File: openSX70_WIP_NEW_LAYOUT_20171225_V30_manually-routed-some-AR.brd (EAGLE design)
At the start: 95.9 x 27.9 mm, 37 parts, among them Q1 5.8A/30V/35mΩ, Q2 5.8A/30V/35mΩ, U1 ATMEGA328P_TQFP, U3 BH1750FVI-TR, Y1 CSTCE16M0V53-R0

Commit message: Added some vias.
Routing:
- net GND: vias 14 -> 17
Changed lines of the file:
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@@
 <via x="24.638" y="21.971" extent="1-16" drill="0.35"/>
 <via x="20.193" y="22.606" extent="1-16" drill="0.35"/>
-<wire x1="67.095" y1="24.169" x2="61.302" y2="26.543" width="0" layer="19" extent="1-1"/>
+<via x="64.643" y="8.636" extent="1-16" drill="0.35"/>
+<via x="70.993" y="15.621" extent="1-16" drill="0.35"/>
+<via x="64.643" y="21.971" extent="1-16" drill="0.35"/>
+<wire x1="64.643" y1="21.971" x2="60.325" y2="23.495" width="0" layer="19" extent="1-1"/>
+<wire x1="67.095" y1="21.59" x2="64.643" y2="21.971" width="0" layer="19" extent="1-1"/>
 <wire x1="74.9935" y1="22.4155" x2="74.295" y2="26.035" width="0" layer="19" extent="1-1"/>
-<wire x1="82.423" y1="18.161" x2="76.47" y2="22.545" width="0" layer="19" extent="1-1"/>
-<wire x1="77.26914375" y1="13.5612" x2="78.400515625" y2="12.429828125" width="0" layer="19" extent="1-1"/>
+<wire x1="70.993" y1="15.621" x2="67.095" y2="21.59" width="0" layer="19" extent="1-1"/>
+<wire x1="78.400515625" y1="12.429828125" x2="77.26914375" y2="13.5612" width="0" layer="19" extent="1-1"/>
 <wire x1="16.5693" y1="9.5279" x2="14.605" y2="8.675" width="0" layer="19" extent="1-16"/>
-<wire x1="71.1175" y1="13.7795" x2="72.0885" y2="8.2575" width="0" layer="19" extent="1-1"/>
 </signal>
 <signal name="6V">

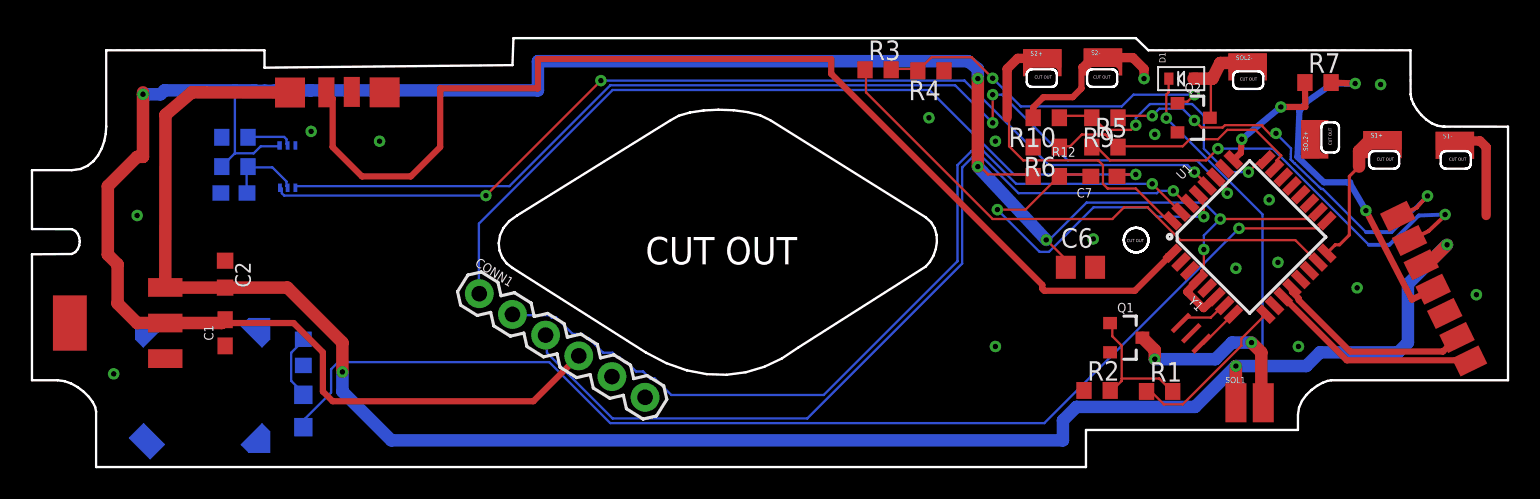
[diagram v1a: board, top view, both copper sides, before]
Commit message: fixed connections on openSX70 library
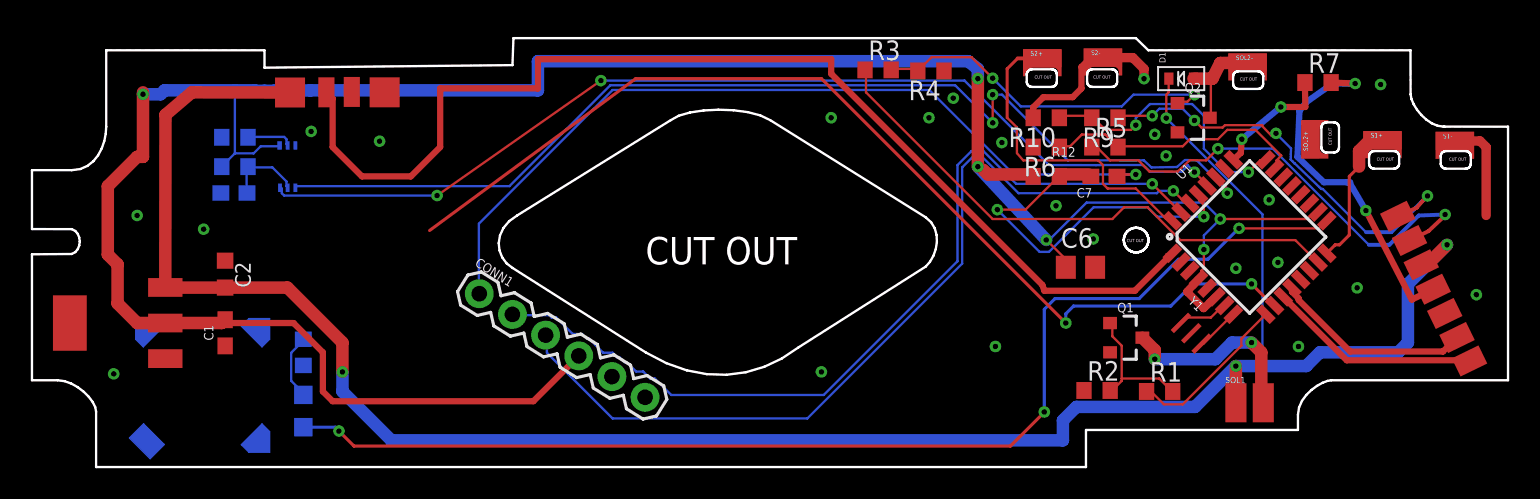
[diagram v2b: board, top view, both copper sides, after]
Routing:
- net BUZZER: track 0.00 -> 68.4 mm, vias 0 -> 2
- net LED: track 76.5 -> 77.2 mm, vias 1 -> 3
- net S9@6V: track 30.0 -> 30.6 mm
- net GND: vias 17 -> 23
